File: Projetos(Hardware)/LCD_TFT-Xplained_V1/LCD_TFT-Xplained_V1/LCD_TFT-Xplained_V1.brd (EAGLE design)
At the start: 69.2 x 83.9 mm, 11 parts

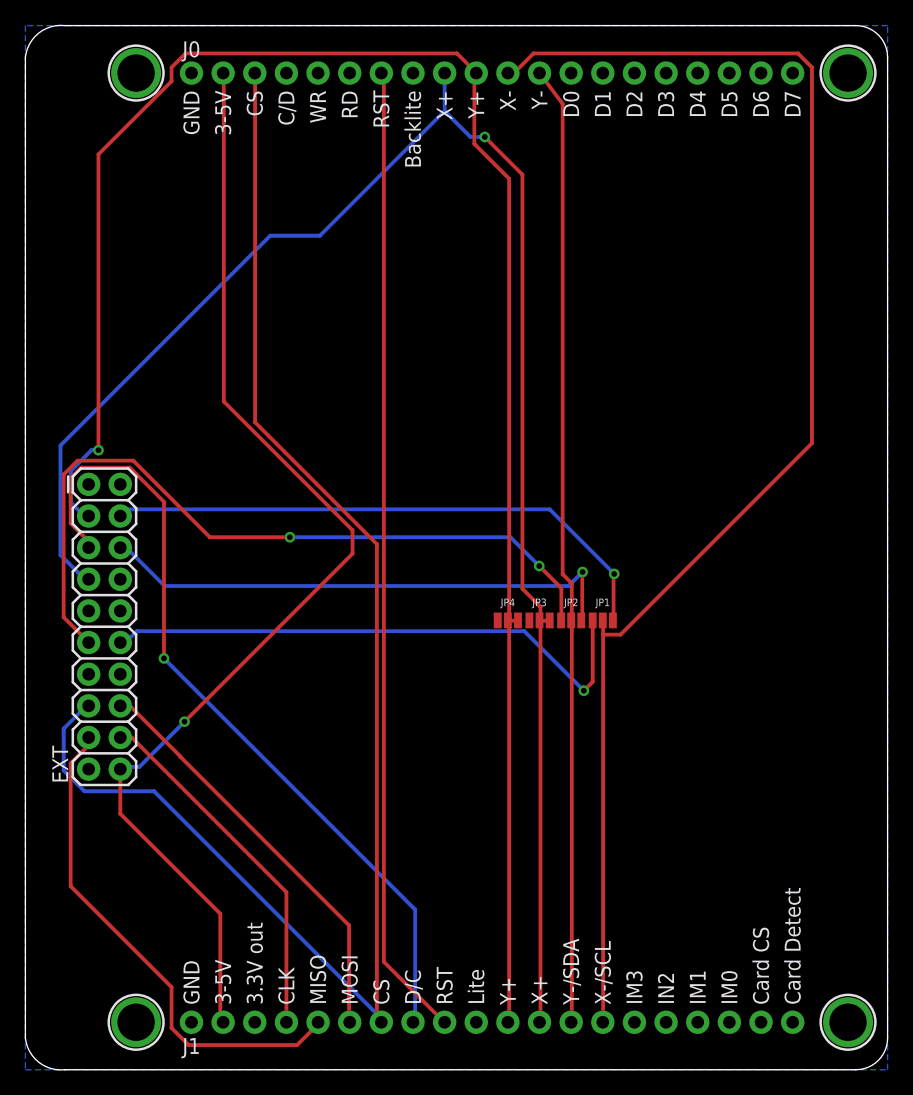
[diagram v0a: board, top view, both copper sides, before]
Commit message: Atualizacao LCD tft
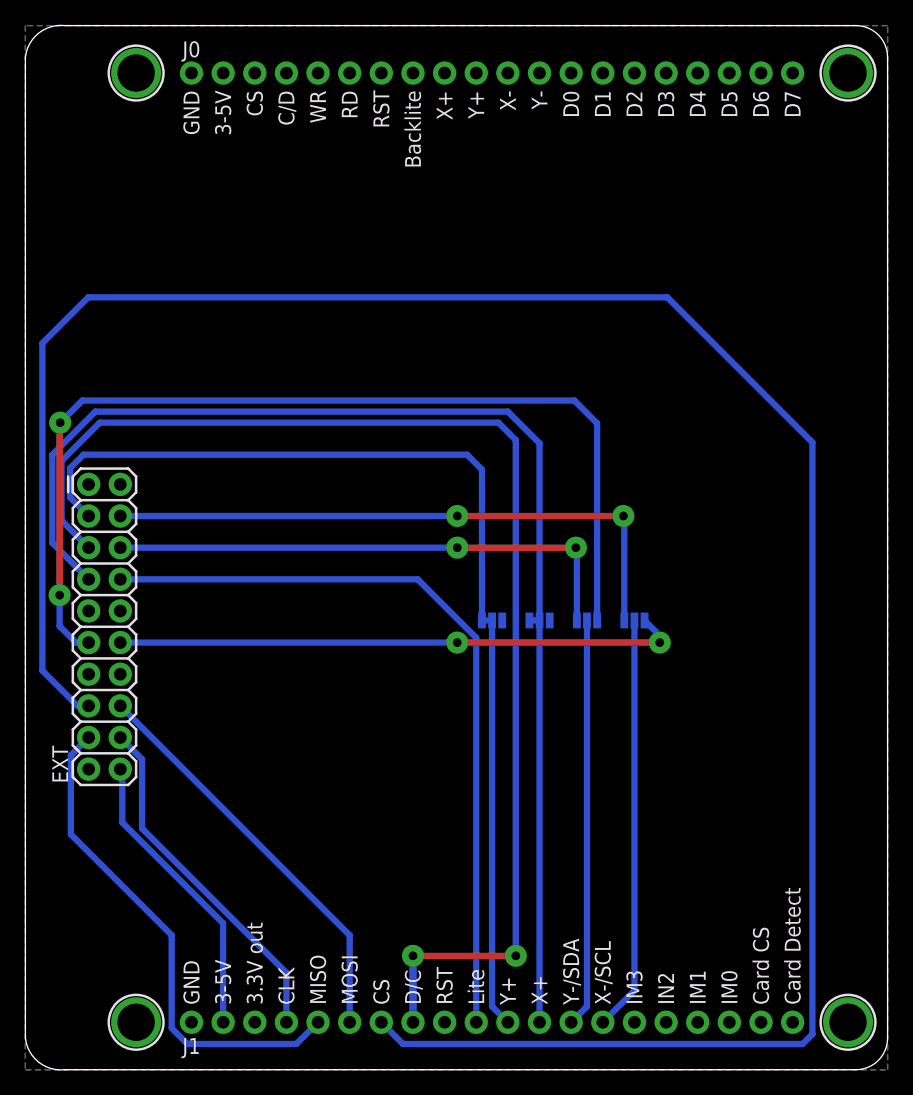
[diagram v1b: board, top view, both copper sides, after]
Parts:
- moved JP1 2.54 mm to (48.9, 36.1), flipped to the bottom
- moved JP2 1.27 mm to (45.1, 36.1), flipped to the bottom
- moved JP4 1.27 mm to (37.5, 36.1), flipped to the bottom
- flipped JP3 to the bottom
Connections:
- removed net N$6: J3.8
- new net CS_OFF: J1.3
- new net GND_OFF: J1.1
- new net RST_OFF: J1.7
- new net VIN_OFF: J1.2
- new net X+_OFF: J1.9
- new net X-/SCL_OFF: J1.11
- new net Y+_OFF: J1.10
- new net Y-/SDA_OFF: J1.12
- net CS: no longer J1.3
- net GND: no longer J1.1
- net LITE: now also J3.8
- net RST: no longer J1.7
- net VIN: no longer J1.2
- net X+: no longer J1.9
- net X-/SCL: no longer J1.11
- net Y+: no longer J1.10
- net Y-/SDA: no longer J1.12
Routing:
- net RST: track 78.4 -> 0.00 mm
- net X-/SCL: track 111.1 -> 33.3 mm
- net VIN: track 92.5 -> 23.7 mm, vias 1 -> 0
- net CS: track 120.7 -> 182.5 mm
- net LITE: track 0.00 -> 61.4 mm
- net Y+: track 144.5 -> 84.2 mm, vias 1 -> 0
- net Y-/SDA: track 77.2 -> 32.8 mm
- net D/C: track 65.4 -> 101.2 mm, vias 1 -> 2
- net X+: track 134.7 -> 100.1 mm, vias 1 -> 0
- net SDA: track 61.6 -> 79.7 mm
- net X-: track 45.8 -> 48.8 mm, vias 1 -> 2
- net CLK: track 28.9 -> 28.4 mm
- net Y-: track 42.8 -> 42.4 mm, vias 1 -> 2
- net SCL: track 45.7 -> 45.6 mm, vias 1 -> 2
- added copper zone on layer 1, net GND
